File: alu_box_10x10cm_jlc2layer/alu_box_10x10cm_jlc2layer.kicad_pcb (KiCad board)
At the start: 2 copper layers, 2 parts

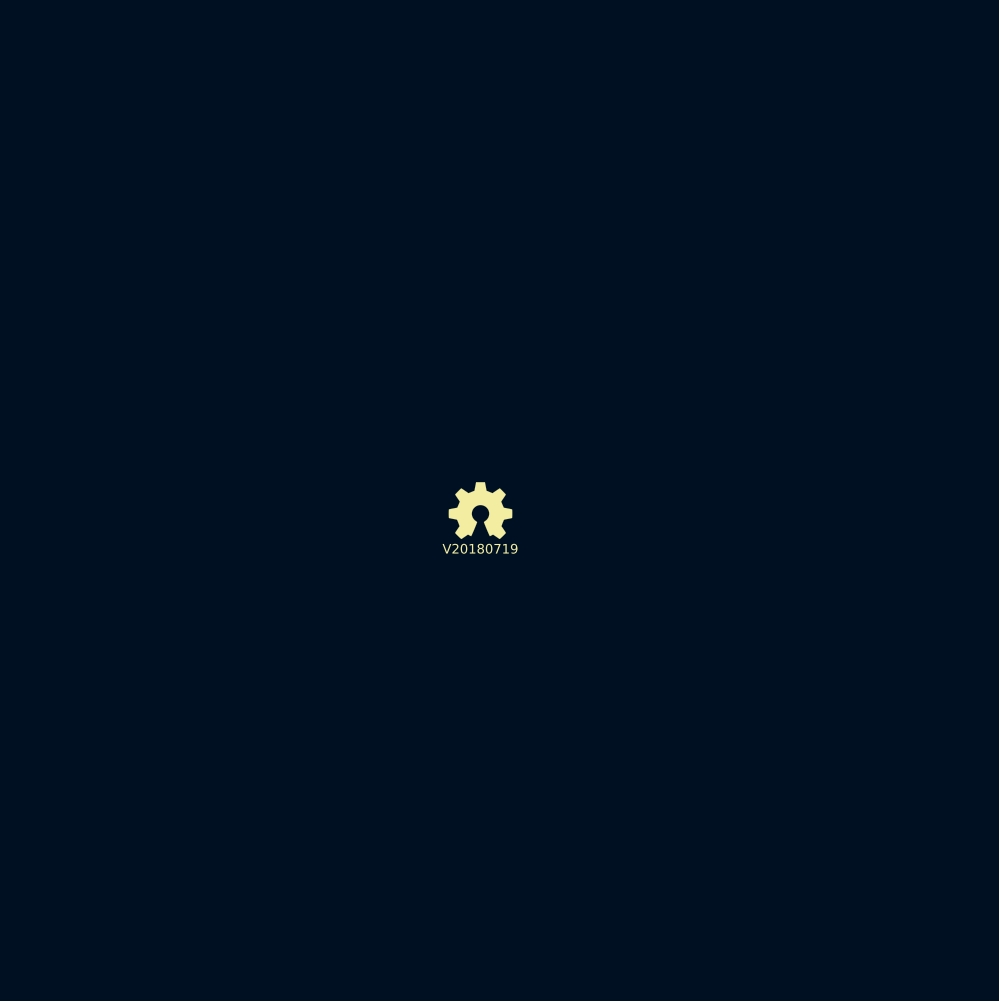
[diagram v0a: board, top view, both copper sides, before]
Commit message: added pcb outlines, still need to check if it is the actual size
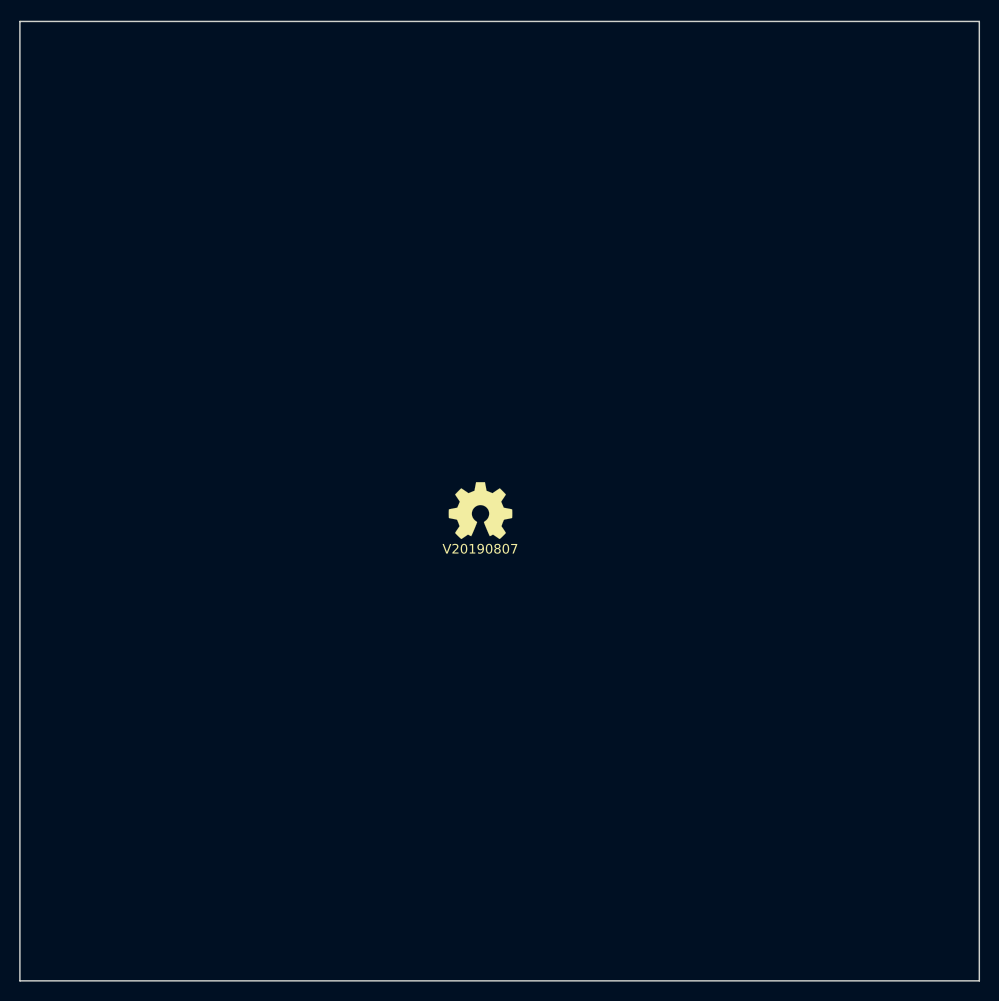
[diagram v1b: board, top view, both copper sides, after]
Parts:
- N2: value V20180719 -> V20190807
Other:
- board outline added: 100 x 100 mm
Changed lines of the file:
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@@
-(kicad_pcb (version 4) (host pcbnew 4.0.7-e2-6376~61~ubuntu18.04.1)
+(kicad_pcb (version 20171130) (host pcbnew 5.1.4-e60b266~84~ubuntu18.04.1)
   (general
-    (links 0)
-    (no_connects 0)
-    (area 0 0 0 0)
     (thickness 1.6)
-    (drawings 0)
+    (drawings 4)
     (tracks 0)
     (zones 0)
@@
     (zone_45_only no)
     (trace_min 0.127)
-    (segment_width 0.2)
-    (edge_width 0.15)
     (via_size 0.6)
     (via_drill 0.3)
@@
     (uvia_min_size 0.381)
     (uvia_min_drill 0.254)
+    (edge_width 0.15)
+    (segment_width 0.2)
     (pcb_text_width 0.3)
     (pcb_text_size 1.5 1.5)
@@
       (layerselection 0x00030_80000001)
       (usegerberextensions false)
+      (usegerberattributes false)
+      (usegerberadvancedattributes false)
+      (creategerberjobfile false)
       (excludeedgelayer true)
       (linewidth 0.100000)
@@
       (hpglpennumber 1)
       (hpglpenspeed 20)
-      (hpglpendiameter 15)
-      (hpglpenoverlay 2)
+      (hpglpendiameter 15.000000)
       (psnegative false)
       (psa4output false)
@@
       (effects (font (size 1 1) (thickness 0.15)))
     )
-    (fp_text value V20180719 (at 0 0) (layer F.SilkS)
-      (effects (font (size 1 1) (thickness 0.15)))
-    )
-  )
+    (fp_text value V20190807 (at 0 0) (layer F.SilkS)
+      (effects (font (size 1 1) (thickness 0.15)))
+    )
+  )
+  (gr_line (start 200 50) (end 200 150) (layer Edge.Cuts) (width 0.15))
+  (gr_line (start 100 150) (end 100 50) (layer Edge.Cuts) (width 0.15))
+  (gr_line (start 200 150) (end 100 150) (layer Edge.Cuts) (width 0.15))
+  (gr_line (start 100 50) (end 200 50) (layer Edge.Cuts) (width 0.15))
 )

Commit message: shrunk pcb, added keepout zones and initial nets
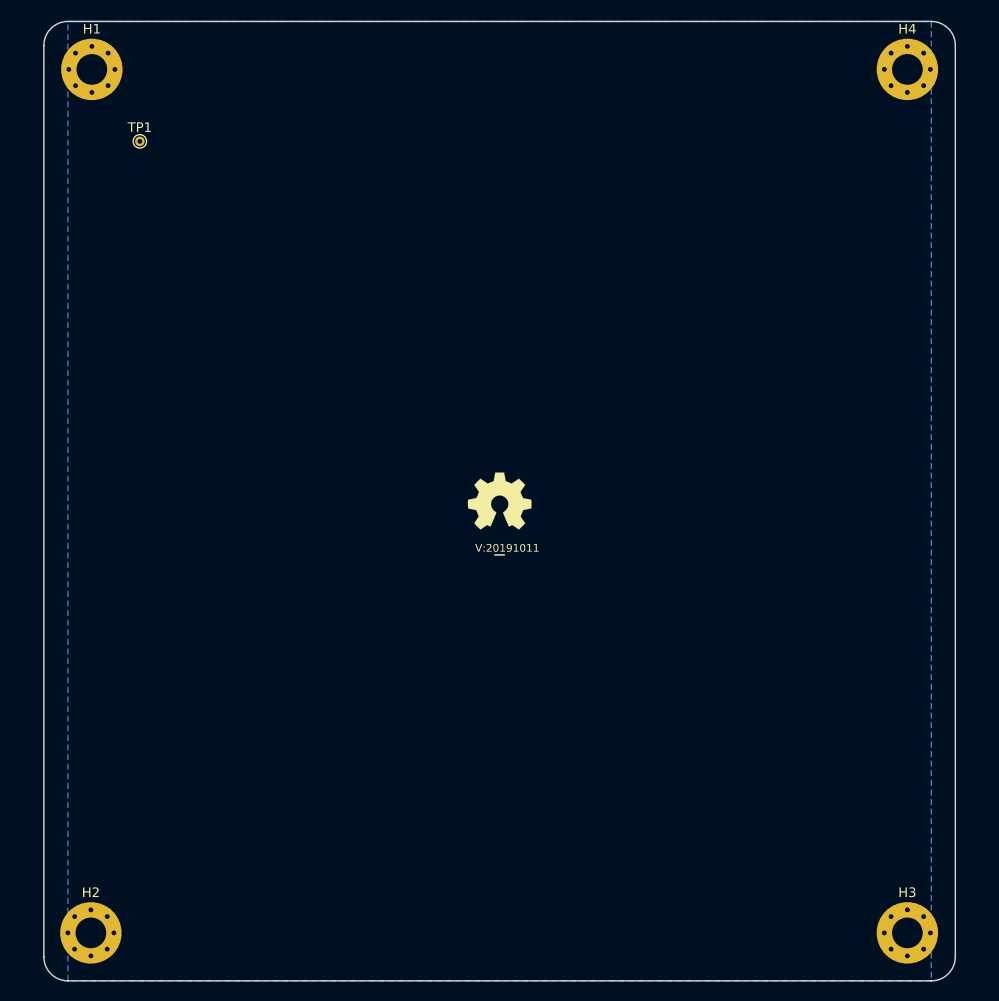
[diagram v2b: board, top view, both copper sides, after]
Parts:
- added H1: M3, MountingHole:MountingHole_3.2mm_M3_Pad_Via, F.Cu at (107.5, 55.0)
- added H2: M3, MountingHole:MountingHole_3.2mm_M3_Pad_Via, F.Cu at (107.4, 145.0)
- added H3: M3, MountingHole:MountingHole_3.2mm_M3_Pad_Via, F.Cu at (192.5, 145.0)
- added H4: M3, MountingHole:MountingHole_3.2mm_M3_Pad_Via, F.Cu at (192.5, 55.0)
- added TP1: testpad, TestPoint:TestPoint_THTPad_D1.0mm_Drill0.5mm, F.Cu at (112.5, 62.5)
- N2: value V20190807 -> V:20191011; footprint SquantorLabels:Label_version -> SquantorLabels:Label_Generic
- moved N1 2.24 mm to (150.0, 100.0)
- moved N2 2.00 mm to (150.0, 105.0)
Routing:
- added copper zone on B.Cu, net /VSS
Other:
- board size 100 x 100 mm -> 95 x 100 mm

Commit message: added one more testpoint so the groundplane is drawn, moved mounting holes, updated versionnumber
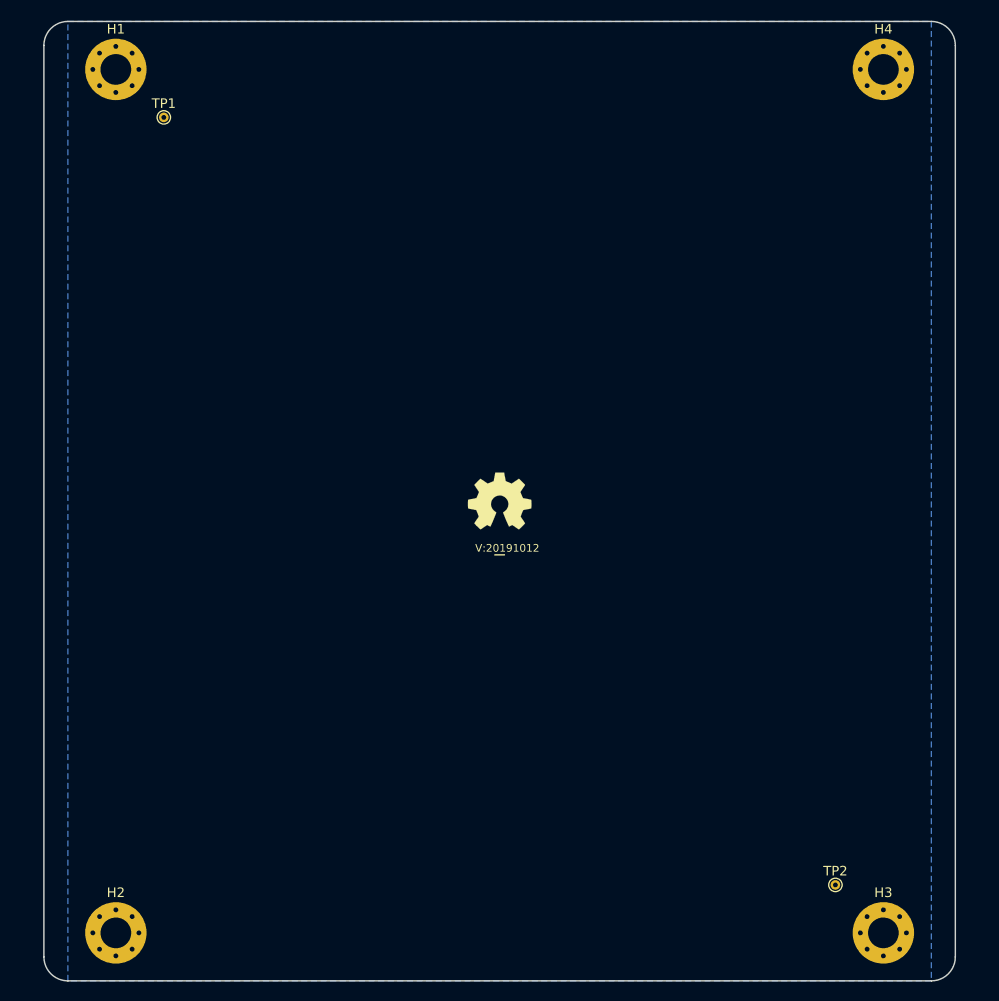
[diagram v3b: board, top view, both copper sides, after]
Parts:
- added TP2: testpad, TestPoint:TestPoint_THTPad_D1.0mm_Drill0.5mm, F.Cu at (185.0, 140.0)
- N2: value V:20191011 -> V:20191012
- moved TP1 3.54 mm to (115.0, 60.0)
- moved H2 2.60 mm to (110.0, 145.0)
- moved H1 2.50 mm to (110.0, 55.0)
- moved H3 2.50 mm to (190.0, 145.0)
- moved H4 2.50 mm to (190.0, 55.0)
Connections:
- TP1 pad 1: (no net) -> /VSS
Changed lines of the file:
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@@
     (tracks 0)
     (zones 0)
-    (modules 7)
+    (modules 8)
     (nets 2)
   )
@@
     (uvia_dia 0.6)
     (uvia_drill 0.3)
+    (add_net /VSS)
   )
   (module TestPoint:TestPoint_THTPad_D1.0mm_Drill0.5mm (layer F.Cu)
-    (at 112.5 62.5)
+    (at 185 140)
     (descr "THT pad as test Point, diameter 1.0mm, hole diameter 0.5mm")
     (tags "test point THT pad")
     (attr virtual)
-    (fp_text reference TP1 (at 0 -1.448) (layer F.SilkS)
+    (fp_text reference TP2 (at 0 -1.448) (layer F.SilkS)
       (effects (font (size 1 1) (thickness 0.15)))
     )
@@
       (effects (font (size 1 1) (thickness 0.15)))
     )
-    (pad 1 thru_hole circle (at 0 0) (size 1 1) (drill 0.5) (layers *.Cu *.Mask))
-  )
-  (module MountingHole:MountingHole_3.2mm_M3_Pad_Via (layer F.Cu)
-    (at 192.5 55)
+    (pad 1 thru_hole circle (at 0 0) (size 1 1) (drill 0.5) (layers *.Cu *.Mask)
+      (net 1 /VSS))
+  )
+  (module TestPoint:TestPoint_THTPad_D1.0mm_Drill0.5mm (layer F.Cu)
+    (at 115 60)
+    (descr "THT pad as test Point, diameter 1.0mm, hole diameter 0.5mm")
+    (tags "test point THT pad")
+    (attr virtual)
+    (fp_text reference TP1 (at 0 -1.448) (layer F.SilkS)
+      (effects (font (size 1 1) (thickness 0.15)))
+    )
+    (fp_text value testpad (at 0 1.55) (layer F.Fab)
+      (effects (font (size 1 1) (thickness 0.15)))
+    )
+    (fp_circle (center 0 0) (end 0 0.7) (layer F.SilkS) (width 0.12))
+    (fp_circle (center 0 0) (end 1 0) (layer F.CrtYd) (width 0.05))
+    (fp_text user %R (at 0 -1.45) (layer F.Fab)
+      (effects (font (size 1 1) (thickness 0.15)))
+    )
+    (pad 1 thru_hole circle (at 0 0) (size 1 1) (drill 0.5) (layers *.Cu *.Mask)
+      (net 1 /VSS))
+  )
+  (module MountingHole:MountingHole_3.2mm_M3_Pad_Via (layer F.Cu)
+    (at 190 55)
     (descr "Mounting Hole 3.2mm, M3")
     (tags "mounting hole 3.2mm m3")
@@
   )
   (module MountingHole:MountingHole_3.2mm_M3_Pad_Via (layer F.Cu)
-    (at 192.5 145)
+    (at 190 145)
     (descr "Mounting Hole 3.2mm, M3")
     (tags "mounting hole 3.2mm m3")
@@
   )
   (module MountingHole:MountingHole_3.2mm_M3_Pad_Via (layer F.Cu)
-    (at 107.4 145)
+    (at 110 145)
     (descr "Mounting Hole 3.2mm, M3")
     (tags "mounting hole 3.2mm m3")
@@
   )
   (module MountingHole:MountingHole_3.2mm_M3_Pad_Via (layer F.Cu)
-    (at 107.5 55)
+    (at 110 55)
     (descr "Mounting Hole 3.2mm, M3")
     (tags "mounting hole 3.2mm m3")
@@
       (effects (font (size 1 1) (thickness 0.15)))
     )
-    (fp_text value V:20191011 (at 0.8 -0.1) (layer F.SilkS)
+    (fp_text value V:20191012 (at 0.8 -0.1) (layer F.SilkS)
       (effects (font (size 0.8 0.8) (thickness 0.15)))
     )

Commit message: WIP: conversion to kicad 6
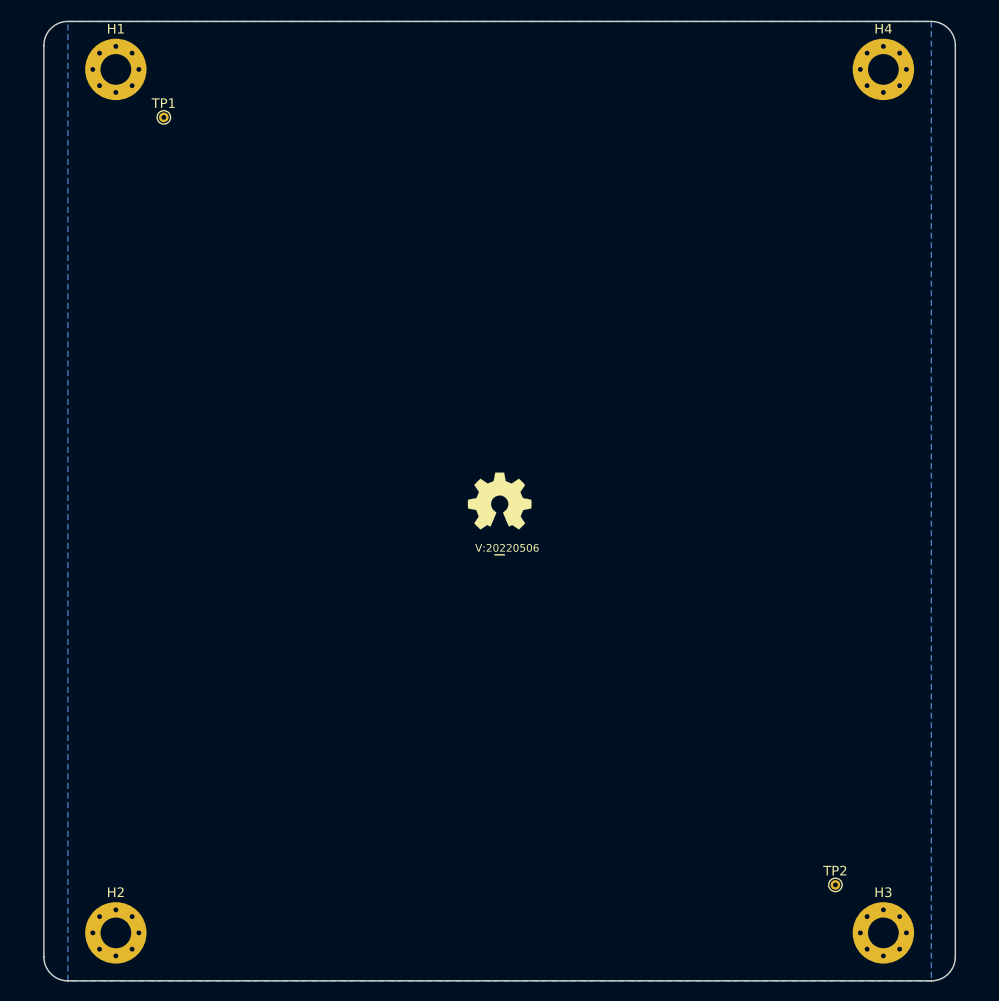
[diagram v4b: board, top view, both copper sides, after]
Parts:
- N2: value V:20191012 -> V:20220506
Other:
- net class Default removed
